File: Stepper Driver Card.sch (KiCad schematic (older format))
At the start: 39 parts, among them J1 Conn_02x22_Top_Bottom, J2 Conn_01x03, J3 Conn_01x03, J4 Conn_01x03, J5 Conn_01x04, J6 Conn_01x04, Q1 STD20NF06L, Q2 STD20NF06L, Q3 STD20NF06L, Q4 STD20NF06L, Q5 STD20NF06L, Q6 STD20NF06L, Q7 STD20NF06L, Q8 STD20NF06L, U2 STM32F030C8Tx, U3 DRV8711

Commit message: worked on motor driver layout
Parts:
- added C10, C11: 18pF, Capacitor_SMD:C_0603_1608Metric_Pad1.05x0.95mm_HandSolder, symbol Device:C
- added C12, C13, C14, C15, C16: 0.1uF, Capacitor_SMD:C_0603_1608Metric_Pad1.05x0.95mm_HandSolder, symbol Device:C
- added D1: LED, LED_SMD:LED_1206_3216Metric_Pad1.42x1.75mm_HandSolder, symbol Device:LED
- added Q9: Q_NMOS_GSD, Package_TO_SOT_SMD:SOT-323_SC-70_Handsoldering, symbol Device:Q_NMOS_GSD
- added R14, R15, R16, R17, R18, R19, R20, R21, R22: 10K, Resistor_SMD:R_0603_1608Metric_Pad1.05x0.95mm_HandSolder, symbol Device:R
- added R23, R24, R25, R26: 0R, Resistor_SMD:R_0603_1608Metric_Pad1.05x0.95mm_HandSolder, symbol Device:R
- added SW1: SW_Push, switches_mdg:FSM2JMTR, symbol Switch:SW_Push
- added TP1, TP2, TP3, TP4, TP5, TP6: TestPoint, test_points_mdg:Keystone_5010, symbol Connector:TestPoint
- added TP10, TP11, TP12, TP7, TP8, TP9: TestPoint, Connector_PinHeader_2.54mm:PinHeader_1x01_P2.54mm_Vertical, symbol Connector:TestPoint
- added Y1: Crystal_GND24, Crystal:Crystal_SMD_SeikoEpson_FA238V-4Pin_3.2x2.5mm_HandSoldering, symbol Device:Crystal_GND24
- U3: footprint Package_SO:TSSOP-38_4.4x9.7mm_P0.5mm -> packages_mdg:TSSOP-38-1_Power_Pad_4.4x9.7mm_P0.5mm
- gave numbers to parts that had none: 1
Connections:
- net +3V3: now also J7.1 (Pin_1), U2.1 (VDD), U2.24 (VDD), U2.48 (VDD), U2.9 (VDDA), C13.2, C14.2, C15.2, C16.2, R15.1, R18.1, R21.1, R22.1
- net AXIS_LIMIT_SWITCH+: now also U2.40 (PB4); no longer U2.28 (PB15)
- net AXIS_LIMIT_SWITCH-: now also U2.39 (PB3); no longer U2.27 (PB14)
- net AXIS_SELECT_X: now also U2.32 (PA11); no longer U2.17 (PA7)
- net AXIS_SELECT_Y: now also U2.33 (PA12); no longer U2.29 (PA8)
- net AXIS_SELECT_Z: now also U2.34 (PA13); no longer U2.30 (PA9)
- net CARD_ENABLE: now also J1.36 (Pin_36), U2.18 (PB0); no longer J1.14 (Pin_14), U2.15 (PA5)
- net CARD_STATUS: now also J1.37 (Pin_37), U2.19 (PB1); no longer J1.15 (Pin_15), U2.16 (PA6)
- net GND: now also J7.3 (Pin_3), J7.5 (Pin_5), J7.9 (Pin_9), U2.23 (VSS), U2.47 (VSS), U2.8 (VSSA), C10.2, C11.2, C12.2, C13.1, C14.1, C15.1, C16.1, Q9.2 (S), R14.2, R17.1, R19.2, R20.1, SW1.1, TP2.1, TP4.1, Y1.2, Y1.4
- net I2C_ADD0: now also J1.33 (Pin_33); no longer J1.11 (Pin_11)
- net I2C_ADD1: now also J1.34 (Pin_34); no longer J1.12 (Pin_12)
- net I2C_ADD2: now also J1.35 (Pin_35); no longer J1.13 (Pin_13)
- net I2C_SCL: now also J1.32 (Pin_32); no longer J1.10 (Pin_10)
- net I2C_SDA: now also J1.31 (Pin_31); no longer J1.9 (Pin_9)
- net BIN2: now reaches J1.16 (Pin_16)
- net BIN2: now also R26.2
- net NRST: now reaches J1.17 (Pin_17)
- net NRST: now also J7.10 (Pin_10), U2.7 (NRST), C12.1, R16.1
- net GPIO_0: now reaches J1.18 (Pin_18)
- net GPIO_0: now also U2.21 (PB10)
- net GPIO_1: now reaches J1.19 (Pin_19)
- net GPIO_1: now also U2.46 (PB9)
- net GPIO_5: now reaches J1.38 (Pin_38)
- net GPIO_5: now also U2.41 (PB5)
- net GPIO_4: now reaches J1.39 (Pin_39)
- net GPIO_4: now also U2.42 (PB6)
- net GPIO_3: now reaches J1.40 (Pin_40)
- net GPIO_3: now also U2.43 (PB7)
- net GPIO_2: now reaches J1.41 (Pin_41)
- net GPIO_2: now also U2.45 (PB8)
- net at U2.2 (PC13): now also TP9.1
- net STATUS_LED: now reaches U2.20 (PB2)
- net STATUS_LED: now also Q9.1 (G), R14.1
- net at U2.22 (PB11): now also TP12.1
- net SPI2_CS: now reaches U2.25 (PB12)
- net SPI2_CS: now also J1.12 (Pin_12)
- net SPI2_SCK: now reaches U2.26 (PB13)
- net SPI2_SCK: now also J1.9 (Pin_9)
- net at U2.3 (PC14): now also TP10.1
- net DRV_RESET: now reaches U2.31 (PA10)
- net DRV_RESET: now also U3.9 (RESET), R20.2
- net at U2.35 (PF6): now also TP7.1
- net at U2.36 (PF7): now also TP8.1
- net DRV_FAULT: now reaches U2.37 (PA14), U3.18 (FAULTn)
- net DRV_FAULT: now also R22.2
- net DRV_STALL: now reaches U2.38 (PA15), U3.19 (STALLn/BEMFVn)
- net DRV_STALL: now also R21.2
- net at U2.4 (PC15): now also TP11.1
- net at U2.44 (BOOT0): now also R17.2
- net at U2.5 (PF0): now also C10.1, Y1.1
- net at U2.6 (PF1): now also C11.1, Y1.3
- net AOUT1: now reaches Q1.3 (S), Q2.2 (D), U3.37 (AOUT1)
- net AOUT1: now also J5.4 (Pin_4); no longer J5.1 (Pin_1)
- net AOUT2: now reaches Q3.2 (D), Q4.3 (S), U3.30 (AOUT2)
- net AOUT2: now also J5.3 (Pin_3); no longer J5.2 (Pin_2)
- net BOUT1: now reaches Q5.3 (S), Q6.2 (D), U3.28 (BOUT1)
- net BOUT1: now also J5.2 (Pin_2); no longer J5.3 (Pin_3)
- net BOUT2: now reaches Q7.2 (D), Q8.3 (S), U3.21 (BOUT2)
- net BOUT2: now also J5.1 (Pin_1); no longer J5.4 (Pin_4)
- net at U3.10 (STEP/AIN1): now also R23.1
- net at U3.11 (DIR/AIN2): now also R24.1
- net at U3.12 (BIN1): now also R25.1
- net at U3.13 (BIN2): now also R26.1
- net B2HS: now reaches R13.2, U3.22 (B2HS)
- net B2LS: now reaches R12.2, U3.23 (B2LS)
- net BISENP: now reaches Q6.3 (S), Q7.3 (S), R11.1, U3.25 (BISENP)
- net B1LS: now reaches R10.2, U3.26 (B1LS)
- net B1HS: now reaches R9.2, U3.27 (B1HS)
- net A2HS: now reaches R8.2, U3.31 (A2HS)
- net A2LS: now reaches R7.2, U3.32 (A2LS)
- net AISENP: now reaches Q2.3 (S), Q3.3 (S), R6.1, U3.34 (AISENP)
- net A1LS: now reaches R5.2, U3.35 (A1LS)
- net A1HS: now reaches R4.2, U3.36 (A1HS)
- net DRV_SLEEP: now reaches U3.8 (SLEEPn)
- net DRV_SLEEP: now also U2.30 (PA9), R19.1
- net SWDIO: now reaches J7.2 (Pin_2)
- net SWCLK: now reaches J7.4 (Pin_4)
- net SWO: now reaches J7.6 (Pin_6)
- net SPI_CS renamed SPI1_CS
- net SPI1_CS: now also U2.29 (PA8), TP3.1; no longer J1.34 (Pin_34)
- net SPI_MISO renamed SPI1_MISO
- net SPI1_MISO: now also U2.16 (PA6), TP1.1; no longer J1.32 (Pin_32)
- net SPI_MOSI renamed SPI1_MOSI
- net SPI1_MOSI: now also U2.17 (PA7), TP5.1; no longer J1.33 (Pin_33)
- net SPI_SCK renamed SPI1_SCK
- net SPI1_SCK: now also U2.15 (PA5), TP6.1; no longer J1.31 (Pin_31)
- new net: R16.2, R18.2, SW1.2
- new net: D1.1 (K), Q9.3 (D)
- new net: D1.2 (A), R15.2
- new net BIN1: J1.15 (Pin_15), R25.2
- new net DIR: J1.14 (Pin_14), R24.2
- new net SPI2_MISO: J1.10 (Pin_10), U2.27 (PB14)
- new net SPI2_MOSI: J1.11 (Pin_11), U2.28 (PB15)
- new net STEP: J1.13 (Pin_13), R23.2
- no-connect marks 0 -> 2
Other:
- moved on the sheet: C1, C2, C3, C4, C5, C6, C7, C8, C9, J5, J6, J7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

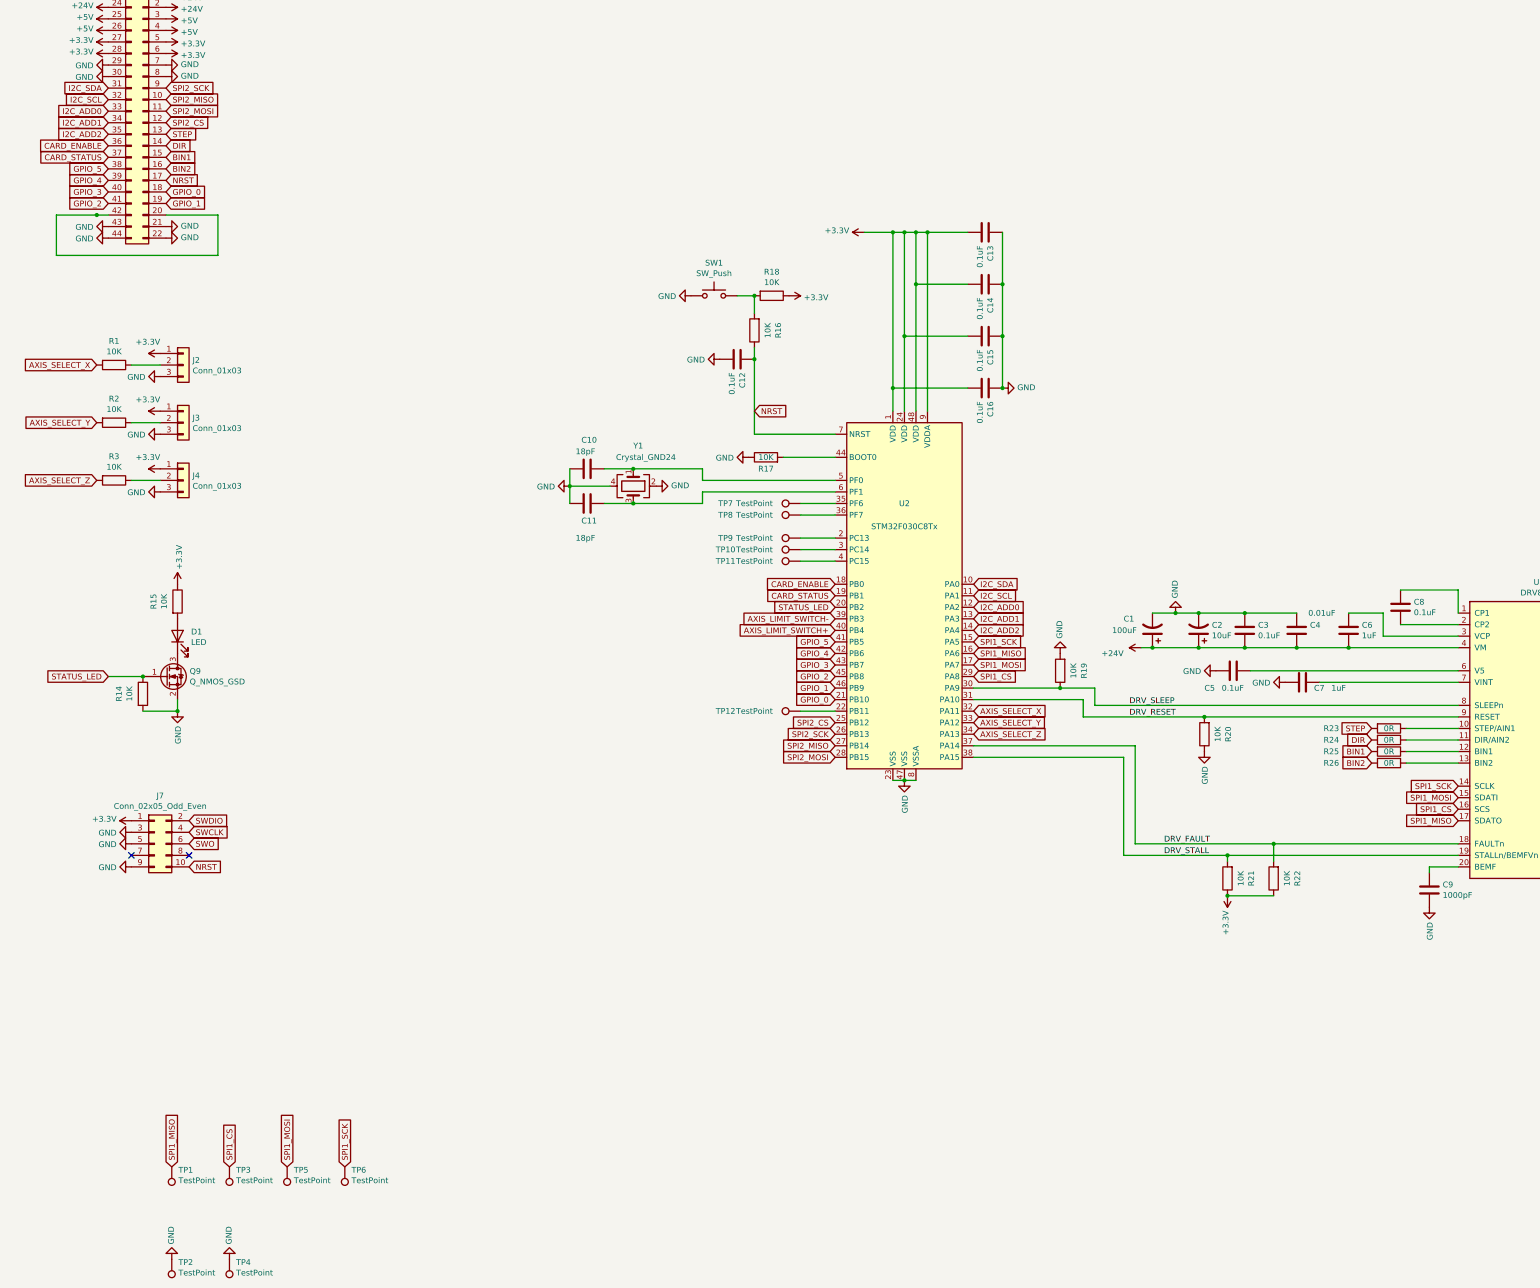
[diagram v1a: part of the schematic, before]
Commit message: All traces connected, board needs to be cleaned up.
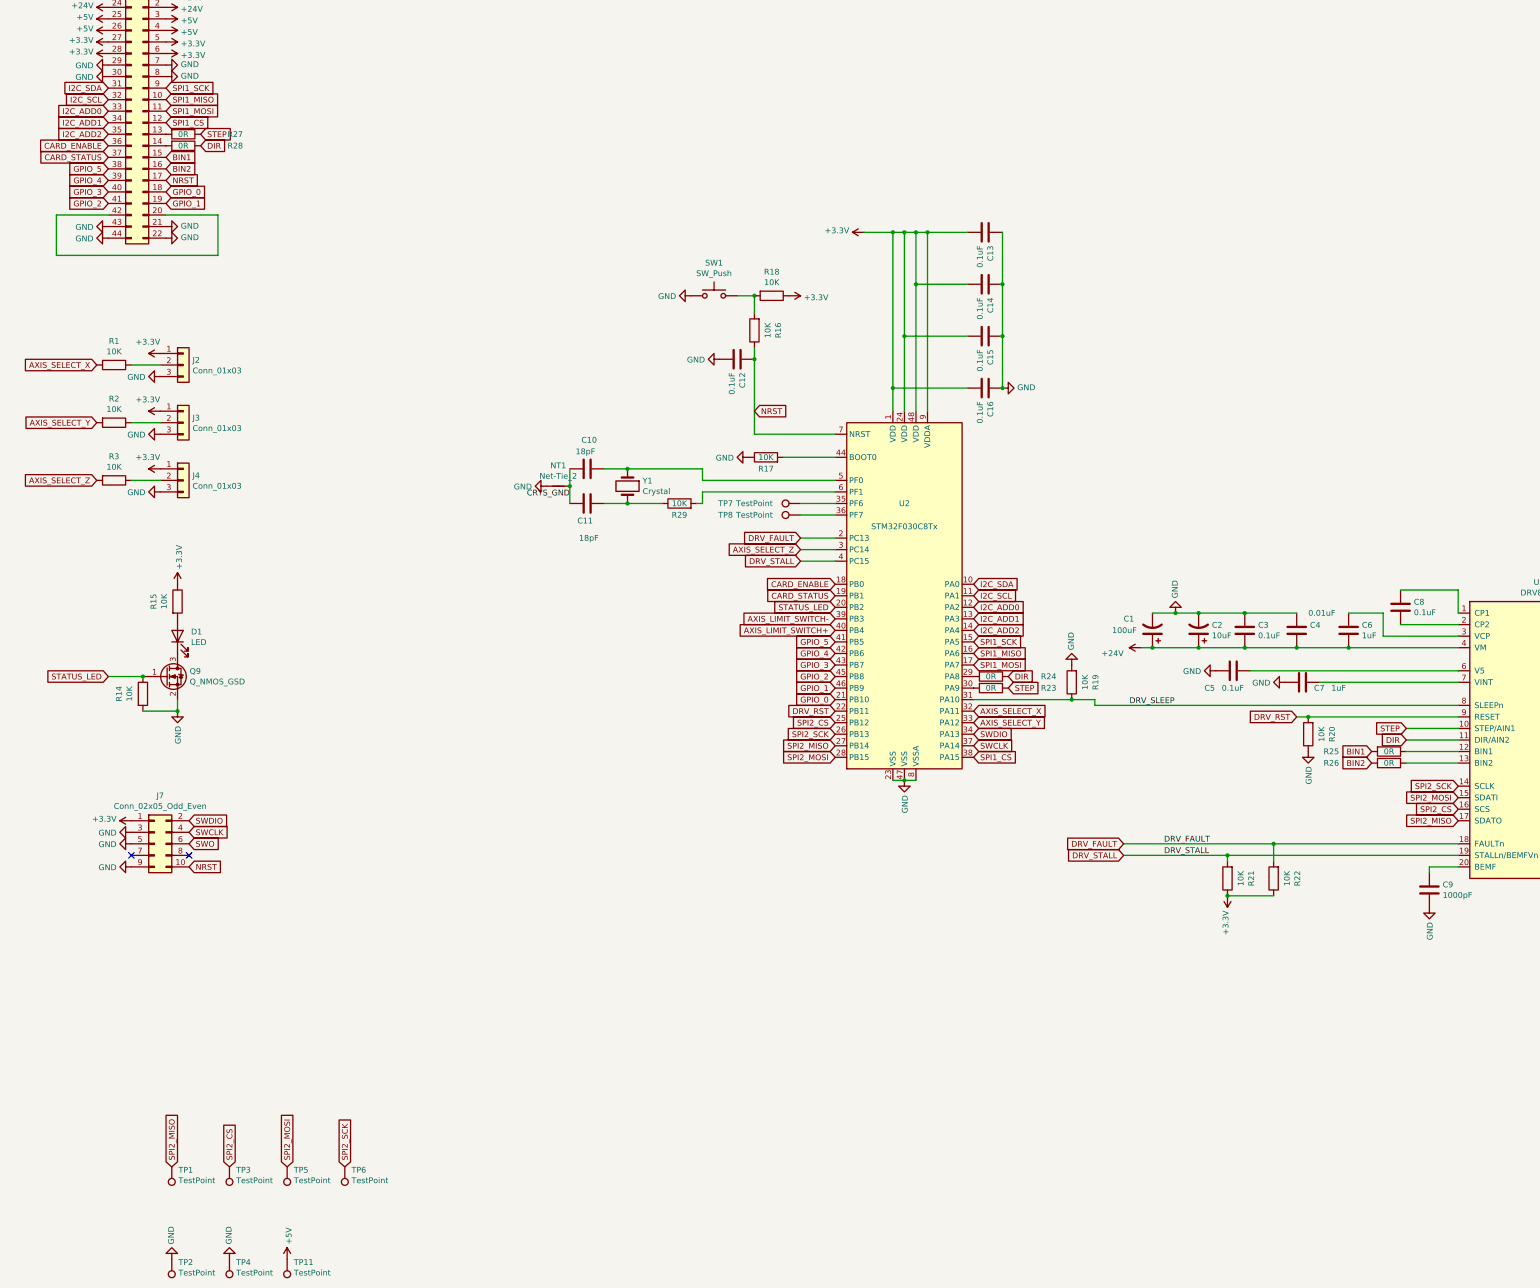
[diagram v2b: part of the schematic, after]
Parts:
- removed TP10, TP12, TP9: TestPoint, Connector_PinHeader_2.54mm:PinHeader_1x01_P2.54mm_Vertical, symbol Connector:TestPoint
- removed Y1: Crystal_GND24, Crystal:Crystal_SMD_SeikoEpson_FA238V-4Pin_3.2x2.5mm_HandSoldering, symbol Device:Crystal_GND24
- added NT1: Net-Tie_2, NetTie:NetTie-2_SMD_Pad0.5mm, symbol Device:Net-Tie_2
- added R27, R28: 0R, Resistor_SMD:R_0603_1608Metric_Pad1.05x0.95mm_HandSolder, symbol Device:R
- added R29: 10K, Resistor_SMD:R_0603_1608Metric_Pad1.05x0.95mm_HandSolder, symbol Device:R
- added Y1: Crystal, Crystal:Crystal_SMD_Abracon_ABM3-2Pin_5.0x3.2mm_HandSoldering, symbol Device:Crystal
- TP1, TP2, TP3, TP4, TP5, TP6: footprint test_points_mdg:Keystone_5010 -> test_points_mdg:TestPoint_Keystone_5015_Micro-Minature
- TP11: footprint Connector_PinHeader_2.54mm:PinHeader_1x01_P2.54mm_Vertical -> test_points_mdg:Keystone_5010
- TP7, TP8: footprint Connector_PinHeader_2.54mm:PinHeader_1x01_P2.54mm_Vertical -> Connector_PinHeader_1.00mm:PinHeader_1x01_P1.00mm_Vertical
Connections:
- net +5V: now also TP11.1
- net AXIS_SELECT_Z: now also U2.3 (PC14); no longer U2.34 (PA13)
- net DIR: now also R24.1, U3.11 (DIR/AIN2), R28.1; no longer J1.14 (Pin_14), R24.2
- net DRV_FAULT: now also U2.2 (PC13); no longer U2.37 (PA14)
- net DRV_SLEEP: now also U2.31 (PA10); no longer U2.30 (PA9)
- net DRV_STALL: now also U2.4 (PC15); no longer U2.38 (PA15)
- net GND: now also NT1.1; no longer C10.2, C11.2
- net SPI1_CS: now also J1.12 (Pin_12), U2.38 (PA15); no longer TP3.1, U2.29 (PA8), U3.16 (SCS)
- net SPI1_MISO: now also J1.10 (Pin_10); no longer TP1.1, U3.17 (SDATO)
- net SPI1_MOSI: now also J1.11 (Pin_11); no longer TP5.1, U3.15 (SDATI)
- net SPI1_SCK: now also J1.9 (Pin_9); no longer TP6.1, U3.14 (SCLK)
- net SPI2_CS: now also TP3.1, U3.16 (SCS); no longer J1.12 (Pin_12)
- net SPI2_MISO: now also TP1.1, U3.17 (SDATO); no longer J1.10 (Pin_10)
- net SPI2_MOSI: now also TP5.1, U3.15 (SDATI); no longer J1.11 (Pin_11)
- net SPI2_SCK: now also TP6.1, U3.14 (SCLK); no longer J1.9 (Pin_9)
- net STEP: now also R23.1, U3.10 (STEP/AIN1), R27.1; no longer J1.13 (Pin_13), R23.2
- net SWCLK: now also U2.37 (PA14)
- net SWDIO: now also U2.34 (PA13)
- net DRV_RST: now reaches U2.22 (PB11)
- net DRV_RST: now also R20.2, U3.9 (RESET)
- net at C10.1, U2.5 (PF0): now also Y1.1
- net at U2.6 (PF1): now also R29.2; no longer C11.1
- removed net DRV_RESET: R20.2, U2.31 (PA10), U3.9 (RESET)
- new net: J1.13 (Pin_13), R27.2
- new net: J1.14 (Pin_14), R28.2
- new net: R24.2, U2.29 (PA8)
- new net: R23.2, U2.30 (PA9)
- new net: C11.2, R29.1, Y1.2
- new net CRYS_GND: C10.2, C11.1, NT1.2
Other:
- moved on the sheet: R19, R20, R23, R24
